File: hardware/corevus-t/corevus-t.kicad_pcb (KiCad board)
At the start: 4 copper layers, 49.8 x 24.2 mm, 50 parts, among them J1 MF3, J10 pinheader, J2 XH, J3 MF3, J4 XH, J5 XH, J6 XH, J7 XH, J8 pinheader, J9 XH, Q1 AO3400, Q2 NMOS, Q3 AO3401A, Q4 AO3400, SW1 RST, SW2 BOOT, U1 LIS2DE12, U2 TPS54302, U3 STM32G431KBU3, U4 TMC2209-LA, Y1 12 MHz

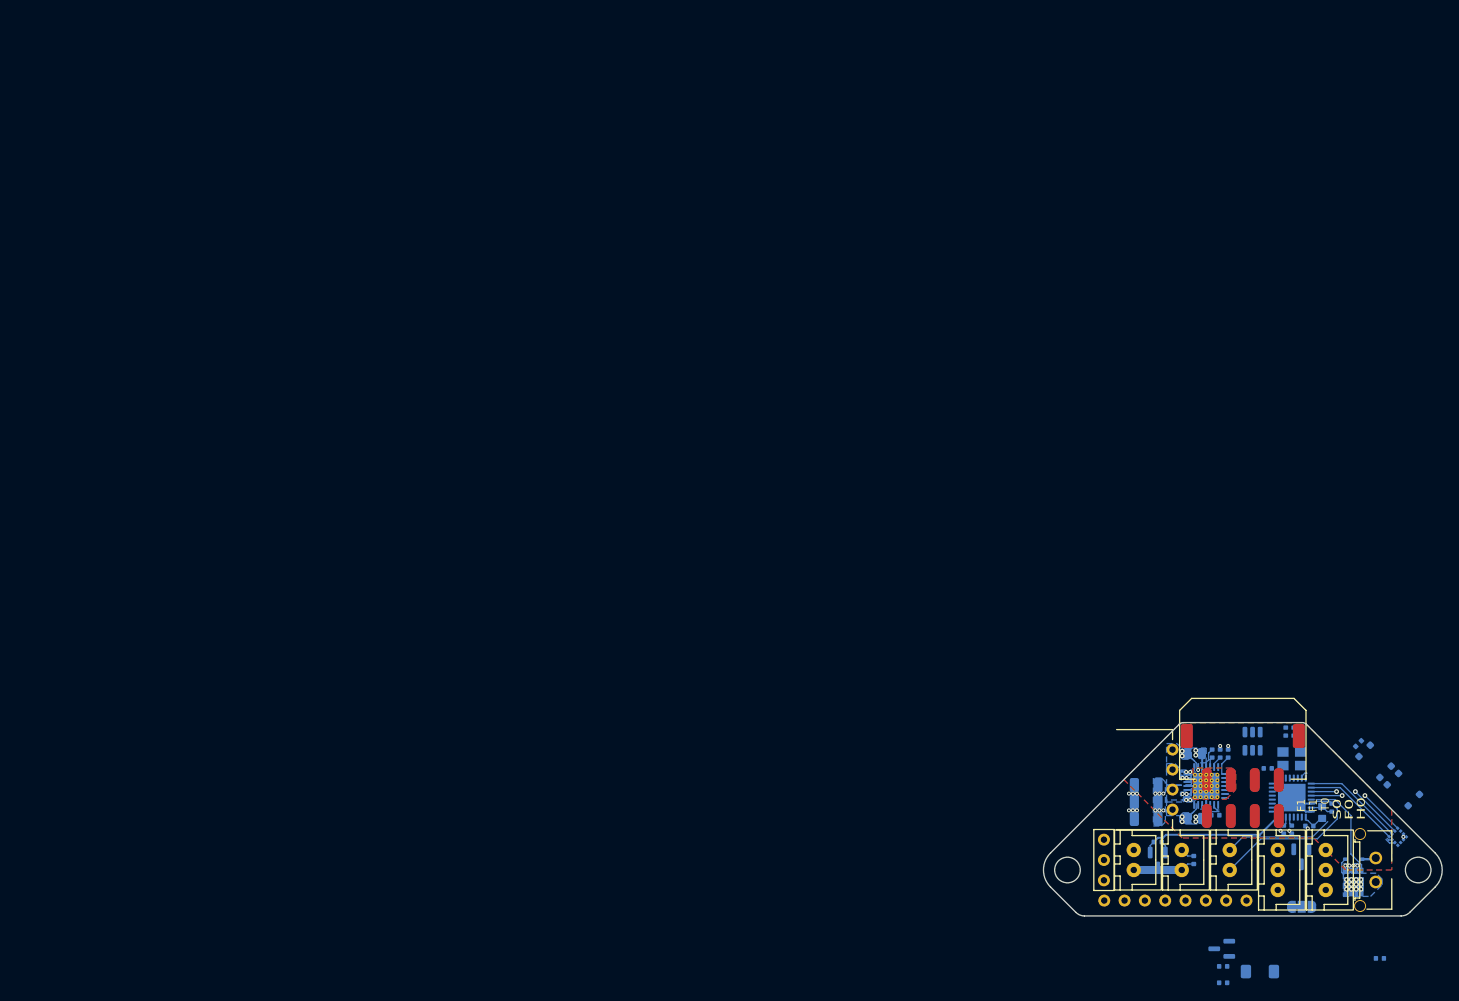
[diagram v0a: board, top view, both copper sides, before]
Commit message: v0.4 mostly complete, board needs minor revisions (e.g. pin swap)
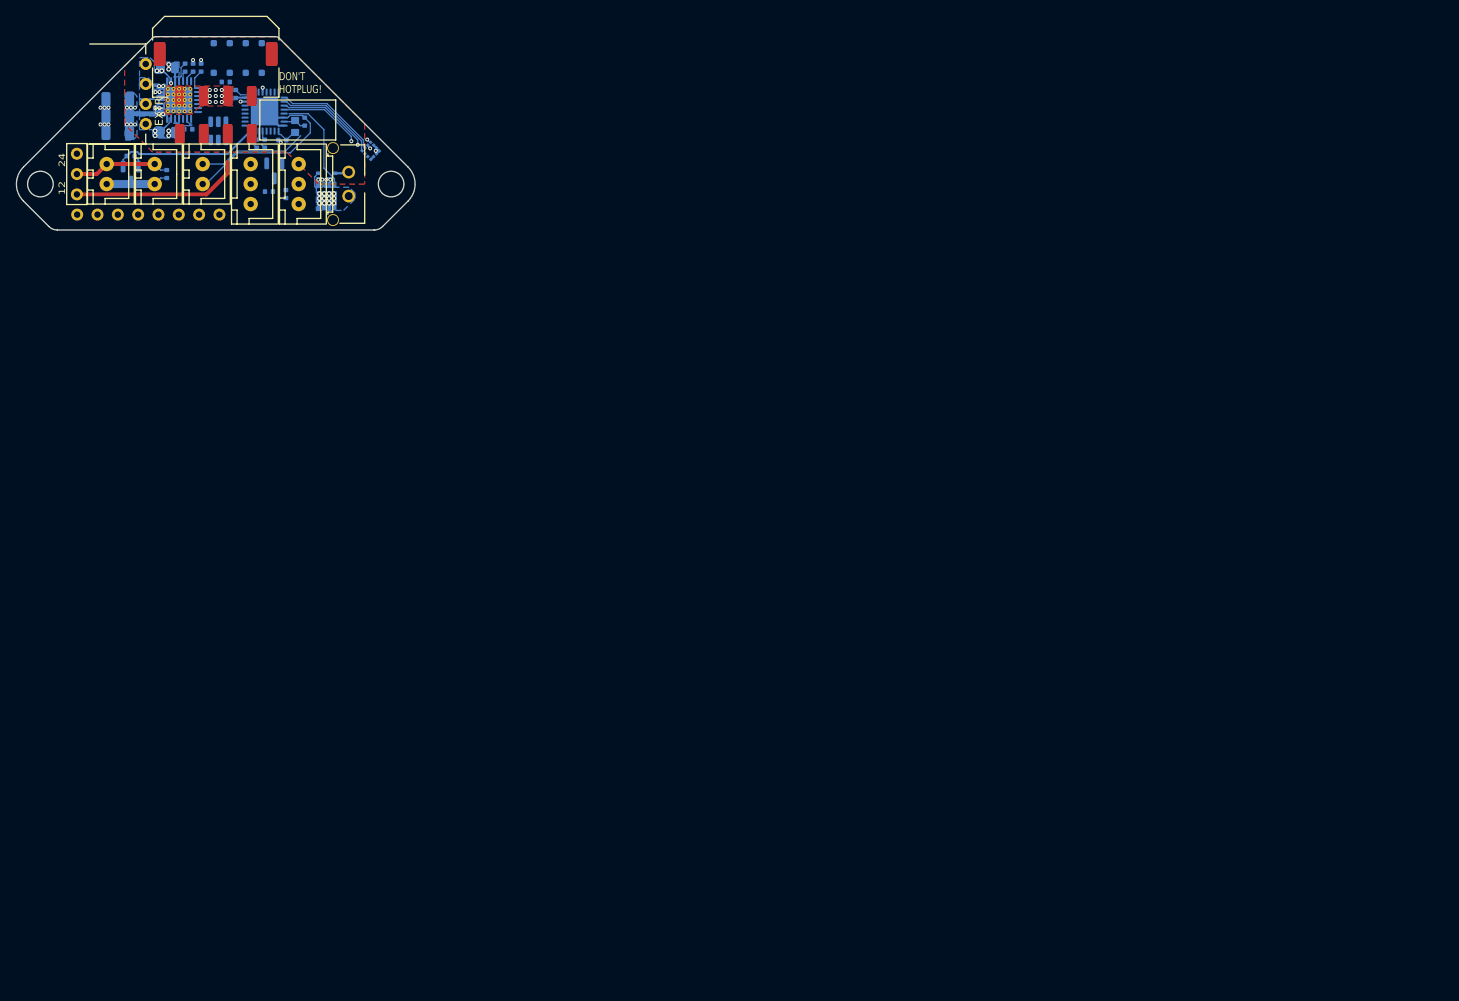
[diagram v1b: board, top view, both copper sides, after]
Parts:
- removed C2, C3: xpF, AlphaLib:0402C
- removed D2: ZMM5V6, Diode_SMD:D_MiniMELF
- removed JP1: F0_V, Jumper:SolderJumper-3_P1.3mm_Bridged12_RoundedPad1.0x1.5mm
- removed Q4: AO3400, Package_TO_SOT_SMD:SOT-23
- removed R8: 1kΩ, AlphaLib:0402R
- removed Y1: 12 MHz, Crystal:Crystal_SMD_3225-4Pin_3.2x2.5mm
- C10: value 100nF 50V -> 1μF
- J10: value pinheader -> 1x3P
- R3, R4: value 33Ω -> 47Ω
- moved SW1 170.3 mm to (4.75, -21.5), turned to -90 degrees
- moved SW2 168.9 mm to (0.75, -21.5), turned to 90 degrees
- moved C10 166.8 mm to (8.77, -4.49), turned to 90 degrees
- moved R2 164.0 mm to (1.25, -18.5), turned to 0 degrees
- moved C14 154.5 mm to (-12.2, -16.3)
- moved C6 154.5 mm to (-12.2, -14.2)
- moved C7 154.5 mm to (-12.2, -12.1)
- moved U3 154.4 mm to (6.10, -14.8)
- moved C1 154.4 mm to (-6.13, -6.99)
- moved C13 154.4 mm to (11.1, -13.5)
- moved C4 154.4 mm to (-1.83, -20.3)
- moved C5 154.4 mm to (-3.43, -12.6)
- moved C8 154.4 mm to (-2.83, -20.3)
- moved C9 154.4 mm to (-3.83, -20.3)
- moved D1 154.4 mm to (13.9, -7.09)
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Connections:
- J10 pad 1: unconnected-(J10-Pin_1-Pad1) -> +24V
- J10 pad 2: unconnected-(J10-Pin_2-Pad2) -> /F1_V+
- J10 pad 3: unconnected-(J10-Pin_3-Pad3) -> +12V
- J3 pad 3: unconnected-(J3-Pin_3-Pad3) -> GND
- J3 pad 7: unconnected-(J3-Pin_7-Pad7) -> +12V
- Q3 pad 1: Net-(D2-A) -> /F0_Gate
- Q3 pad 2: Net-(D2-K) -> +5V
- R7 pad 1: Net-(D2-K) -> /F0_Gate
- R7 pad 2: Net-(D2-A) -> GND
- U1 pad 10: unconnected-(U1-Vdd_IO-Pad10) -> +3.3V
- U1 pad 5: unconnected-(U1-RES-Pad5) -> GND
- U1 pad 9: unconnected-(U1-Vdd-Pad9) -> +3.3V
- U2 pad 1: unconnected-(U2-GND-Pad1) -> GND
- U2 pad 3: unconnected-(U2-VIN-Pad3) -> +12V
- U3 pad 2: Net-(U3-PF0) -> unconnected-(U3-PF0-Pad2)
- U3 pad 3: Net-(U3-PF1) -> unconnected-(U3-PF1-Pad3)
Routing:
- net +12V: track 0.00 -> 21.3 mm
- net /F1_V+: track 2.06 -> 12.3 mm
- net GND: track 11.8 -> 17.7 mm, vias 17 -> 26
- net +24V: track 2.21 -> 6.31 mm
- net +3.3V: track 2.68 -> 5.30 mm
- net /MISO: track 12.5 -> 13.8 mm
- net /INT2: track 1.32 -> 0.00 mm
- net unconnected-(U3-PA2-Pad7): track 1.04 -> 0.00 mm
- net /INT1: track 0.72 -> 0.00 mm
- net /SCK: track 12.3 -> 13.0 mm
- net /~{Reset}: track 0.00 -> 0.56 mm, vias 0 -> 1
- net /BOOT0: track 0.00 -> 0.56 mm, vias 0 -> 1
- net /MOSI: track 12.5 -> 13.0 mm
- net Net-(J3-Pin_8): track 0.54 -> 0.49 mm, vias 1 -> 0
- net Net-(J3-Pin_4): track 0.47 -> 0.49 mm, vias 1 -> 0
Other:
- board text added: "12"
- board text added: "24"
- board text added: "DON'T HOTPLUG!"
- board text added: "EXTR"
- board text removed: "F0"
- board text removed: "F1"
- board text removed: "H0"
- board text removed: "S0"
- board text removed: "T0"
